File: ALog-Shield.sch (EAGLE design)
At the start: 28 parts, among them U1 DS3231MZ/V+T

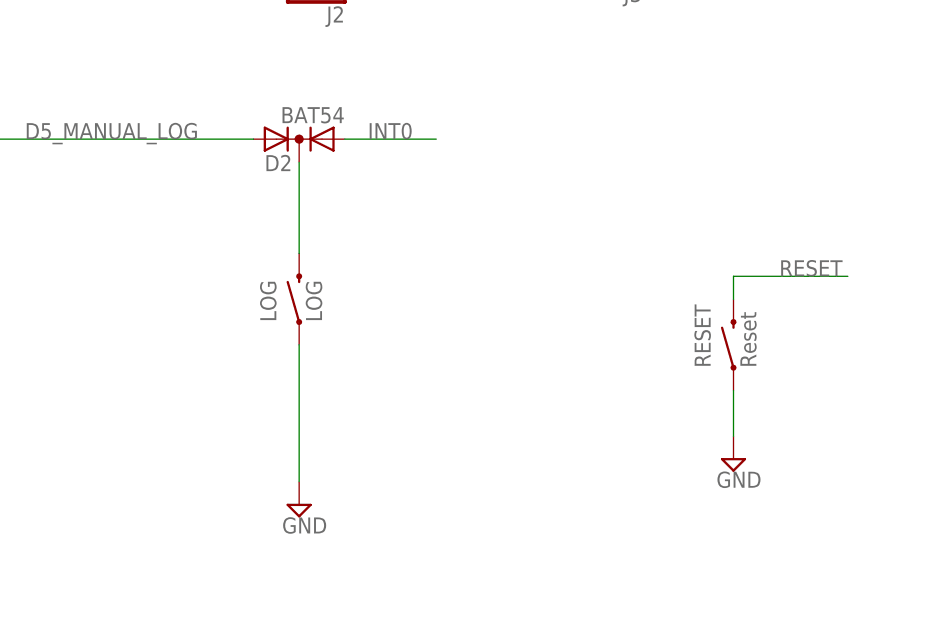
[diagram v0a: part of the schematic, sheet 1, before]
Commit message: New buttons: consistent with TLog
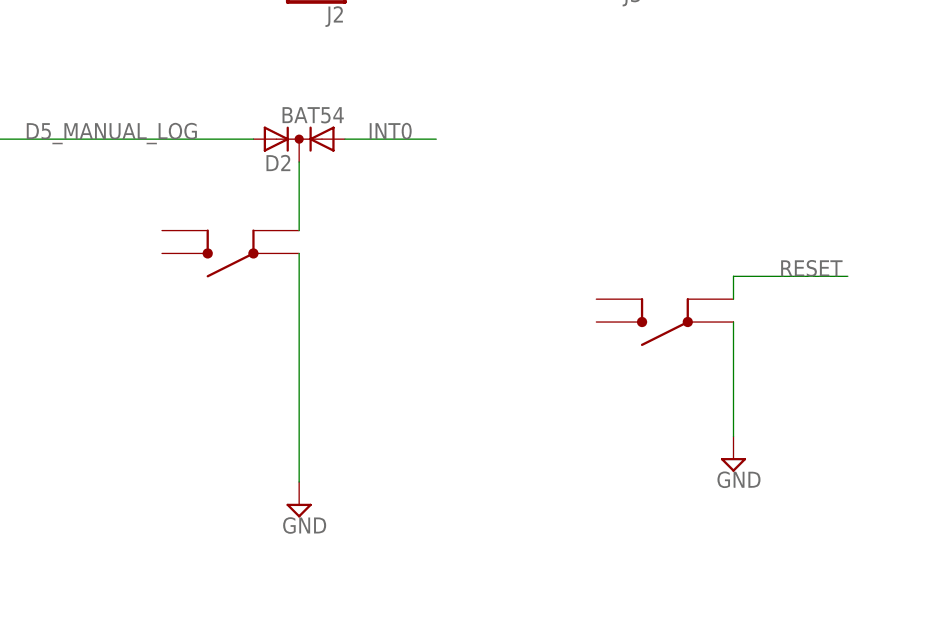
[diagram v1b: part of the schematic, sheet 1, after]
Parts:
- LOG, RESET: device SparkFun-Electromechanical:SWITCH-MOMENTARY-2PTH -> bschulz:BUTTON4.2X3.2
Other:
- note added: "JUMPER: REFERENCE ANALOG TO 3V3 INSTEAD OF VCC"
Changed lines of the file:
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@@
 <part name="SUPPLY47" library="supply2" deviceset="GND" device=""/>
 <part name="SUPPLY52" library="supply2" deviceset="GND" device=""/>
-<part name="RESET" library="SparkFun-Electromechanical" deviceset="SWITCH-MOMENTARY-2" device="PTH" value="Reset"/>
+<part name="RESET" library="bschulz" deviceset="BUTTON" device="4.2X3.2" value="Reset"/>
 <part name="SUPPLY53" library="supply2" deviceset="GND" device=""/>
 <part name="CLOCK_BATT_DECOUP" library="rcl" deviceset="C-EU" device="C0603" value="0.1uF"/>
 <part name="SUPPLY56" library="supply2" deviceset="GND" device=""/>
 <part name="D2" library="semicon-smd-ipc" deviceset="DIODE_AC-CA_" device="" value="BAT54"/>
-<part name="LOG" library="SparkFun-Electromechanical" deviceset="SWITCH-MOMENTARY-2" device="PTH" value="LOG"/>
+<part name="LOG" library="bschulz" deviceset="BUTTON" device="4.2X3.2" value="LOG"/>
 <part name="U1" library="Maxim-DS3231MZ_8-SOIC" deviceset="DS3231MZ/V+T" device=""/>
 <part name="FRAME1" library="frames" deviceset="LETTER_P" device=""/>
@@
 <instance part="SUPPLY47" gate="GND" x="20.32" y="-177.8"/>
 <instance part="SUPPLY52" gate="GND" x="109.22" y="-200.66"/>
-<instance part="RESET" gate="G$1" x="157.48" y="-182.88" rot="R90"/>
+<instance part="RESET" gate="G$1" x="157.48" y="-180.34" rot="R180"/>
 <instance part="SUPPLY53" gate="GND" x="63.5" y="-208.28"/>
 <instance part="D2" gate="G$1" x="109.22" y="-160.02" rot="R180"/>
-<instance part="LOG" gate="G$1" x="109.22" y="-177.8" rot="R90"/>
+<instance part="LOG" gate="G$1" x="109.22" y="-172.72" rot="R180"/>
 <instance part="FRAME1" gate="G$1" x="0" y="-248.92"/>
 <instance part="FRAME1" gate="G$2" x="83.82" y="-248.92" smashed="yes">
@@
 </segment>
 <segment>
-<wire x1="157.48" y1="-187.96" x2="157.48" y2="-193.04" width="0.1524" layer="91"/>
+<wire x1="157.48" y1="-180.34" x2="157.48" y2="-193.04" width="0.1524" layer="91"/>
 <pinref part="SUPPLY31" gate="GND" pin="GND"/>
 <pinref part="RESET" gate="G$1" pin="1"/>
@@
 <segment>
 <pinref part="SUPPLY52" gate="GND" pin="GND"/>
-<wire x1="109.22" y1="-182.88" x2="109.22" y2="-198.12" width="0.1524" layer="91"/>
+<wire x1="109.22" y1="-172.72" x2="109.22" y2="-198.12" width="0.1524" layer="91"/>
 <pinref part="LOG" gate="G$1" pin="1"/>
 </segment>
@@
 <pinref part="LOG" gate="G$1" pin="2"/>
 <pinref part="D2" gate="G$1" pin="K"/>
-<wire x1="109.22" y1="-172.72" x2="109.22" y2="-162.56" width="0.1524" layer="91"/>
+<wire x1="109.22" y1="-170.18" x2="109.22" y2="-162.56" width="0.1524" layer="91"/>
 </segment>
 </net>
@@
 <text x="90.17" y="26.416" size="5.08" layer="97">ALOG</text>
 <text x="170.942" y="1.016" size="2.54" layer="97">2/2</text>
-<wire x1="0" y1="81.28" x2="185.42" y2="81.28" width="0.1524" layer="97" style="dashdot"/>
+<wire x1="0" y1="81.28" x2="104.14" y2="81.28" width="0.1524" layer="97" style="dashdot"/>
 <text x="152.4" y="27.94" size="1.778" layer="97">Andrew Wickert
 Chad Sandell</text>
@@
 http://creativecommons.org/licenses/by-sa/3.0
 Design by: Andrew D. Wickert and Chad T. Sandell</text>
+<wire x1="104.14" y1="81.28" x2="185.42" y2="81.28" width="0.1524" layer="97" style="dashdot"/>
+<wire x1="104.14" y1="35.56" x2="104.14" y2="81.28" width="0.1524" layer="97" style="dashdot"/>
+<text x="114.3" y="76.2" size="1.778" layer="97">JUMPER: REFERENCE ANALOG TO 3V3 INSTEAD OF VCC</text>
 </plain>
 <instances>

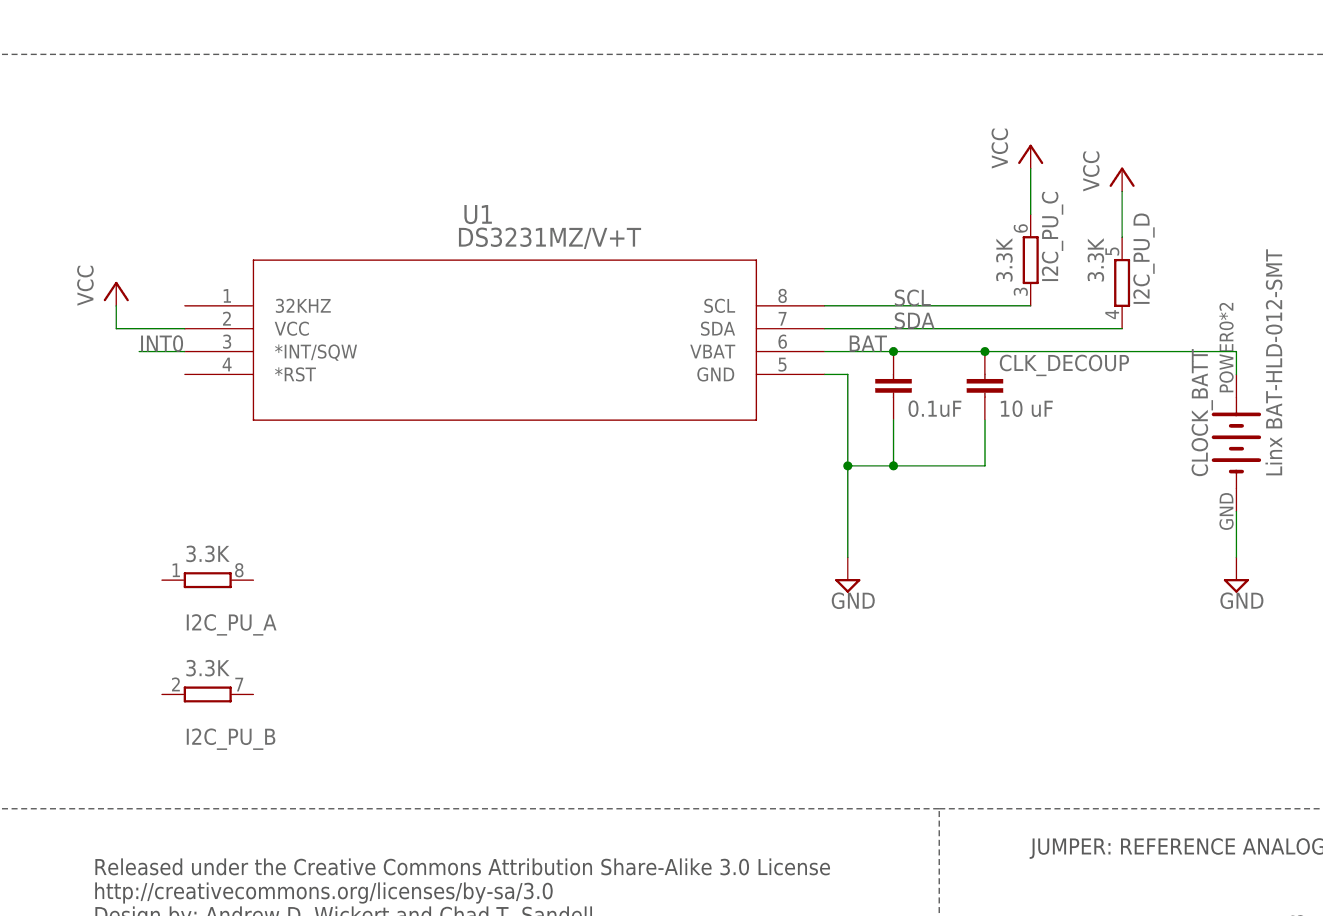
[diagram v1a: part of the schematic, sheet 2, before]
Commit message: 3.3K RTC PU array to discrete (10K?)
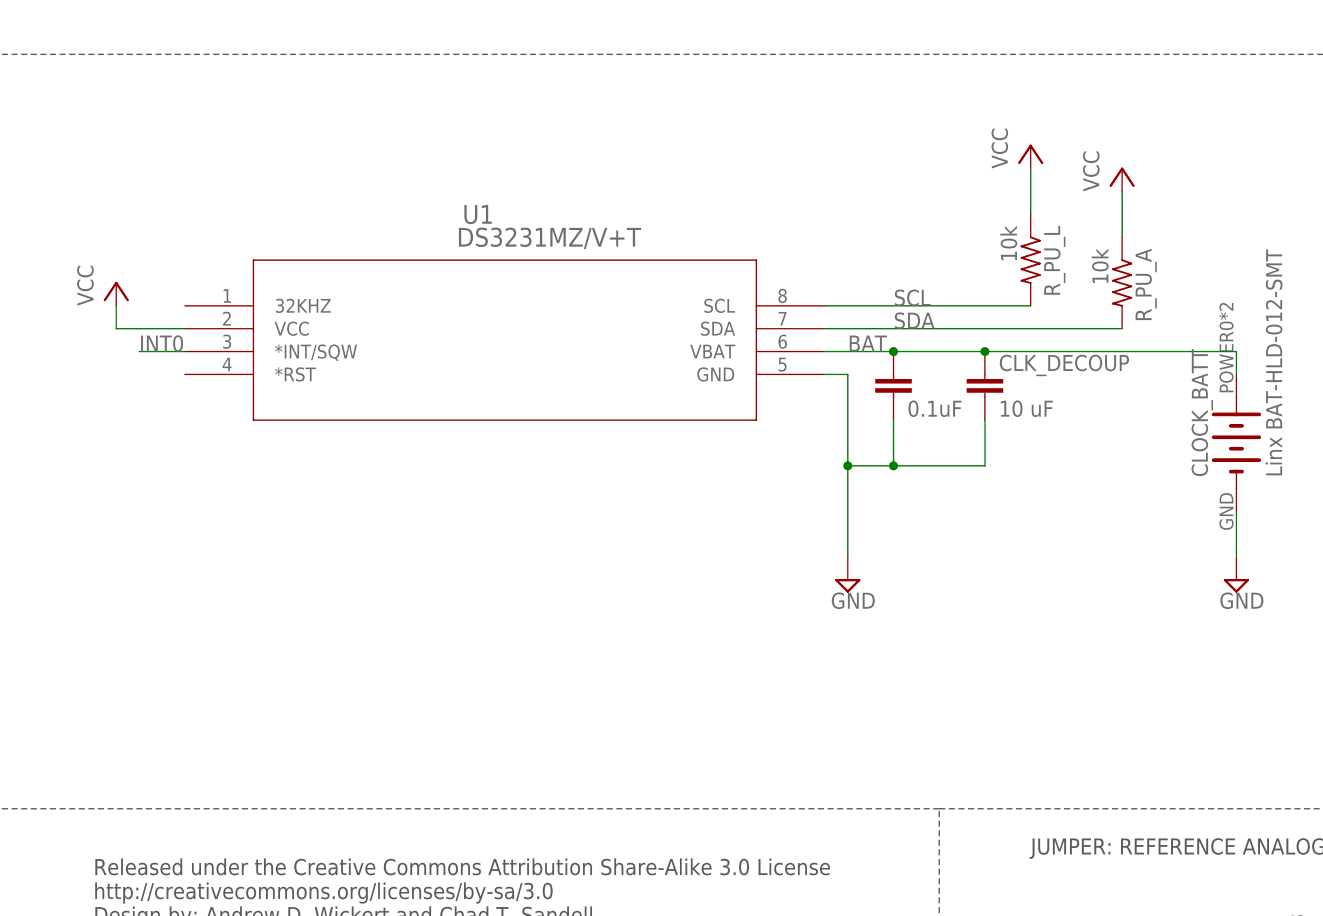
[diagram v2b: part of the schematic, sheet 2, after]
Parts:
- removed I2C_PU_: 3.3K, resistor-dil:4R-N0603-ARC
- added R_PU_A, R_PU_L: 10k, resistor:R-US_R0603
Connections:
- net SCL: now also R_PU_L.2; no longer I2C_PU_C.1
- net SDA: now also R_PU_A.2; no longer I2C_PU_D.1
- net VCC: now also R_PU_A.1, R_PU_L.1; no longer I2C_PU_C.2, I2C_PU_D.2
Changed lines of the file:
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@@
 <?xml version="1.0" encoding="utf-8"?>
 <!DOCTYPE eagle SYSTEM "eagle.dtd">
-<eagle version="8.3.1">
+<eagle version="8.5.0">
 <drawing>
 <settings>
@@
 <part name="SUPPLY3" library="supply2" deviceset="GND" device=""/>
 <part name="J2" library="SparkFun-Connectors" deviceset="CONN_04" device="SCREW"/>
-<part name="I2C_PU_" library="resistor-dil" deviceset="4R-N" device="0603-ARC" value="3.3K"/>
 <part name="C15" library="rc-master-smd" deviceset="CCA_" device="" value="10nF"/>
 <part name="CLOCK_BATT" library="awickert" deviceset="LINX-BAT-HLD-012-SMT-OTL" device="" value="Linx BAT-HLD-012-SMT"/>
@@
 <part name="JP1" library="SparkFun-Connectors" deviceset="M02" device="LOCK"/>
 <part name="+3V3" library="supply1" deviceset="+3V3" device=""/>
+<part name="R_PU_L" library="resistor" deviceset="R-US_" device="R0603" value="10k"/>
+<part name="R_PU_A" library="resistor" deviceset="R-US_" device="R0603" value="10k"/>
 </parts>
 <sheets>
@@
 <instance part="P+7" gate="VCC" x="114.3" y="154.94"/>
 <instance part="P+9" gate="VCC" x="12.7" y="139.7"/>
-<instance part="I2C_PU_" gate="A" x="22.86" y="106.68" smashed="yes">
-<attribute name="VALUE" x="20.32" y="108.712" size="1.778" layer="96"/>
-<attribute name="NAME" x="20.32" y="101.092" size="1.778" layer="95"/>
-</instance>
-<instance part="I2C_PU_" gate="B" x="22.86" y="93.98" smashed="yes">
-<attribute name="VALUE" x="20.32" y="96.012" size="1.778" layer="96"/>
-<attribute name="NAME" x="20.32" y="88.392" size="1.778" layer="95"/>
-</instance>
-<instance part="I2C_PU_" gate="C" x="114.3" y="142.24" smashed="yes" rot="R90">
-<attribute name="VALUE" x="112.268" y="139.7" size="1.778" layer="96" rot="R90"/>
-<attribute name="NAME" x="117.348" y="139.7" size="1.778" layer="95" rot="R90"/>
-</instance>
-<instance part="I2C_PU_" gate="D" x="124.46" y="139.7" smashed="yes" rot="R90">
-<attribute name="VALUE" x="122.428" y="139.7" size="1.778" layer="96" rot="R90"/>
-<attribute name="NAME" x="127.508" y="137.16" size="1.778" layer="95" rot="R90"/>
-</instance>
 <instance part="CLOCK_BATT" gate="G$1" x="137.16" y="121.92" rot="R90"/>
 <instance part="+3V2" gate="G$1" x="60.96" y="215.9"/>
@@
 <instance part="JP1" gate="G$1" x="129.54" y="58.42"/>
 <instance part="+3V3" gate="G$1" x="147.32" y="68.58"/>
+<instance part="R_PU_L" gate="G$1" x="114.3" y="142.24" rot="R270"/>
+<instance part="R_PU_A" gate="G$1" x="124.46" y="139.7" rot="R270"/>
 </instances>
 <busses>
@@
 <wire x1="124.46" y1="149.86" x2="124.46" y2="144.78" width="0.1524" layer="91"/>
 <pinref part="P+5" gate="VCC" pin="VCC"/>
-<pinref part="I2C_PU_" gate="D" pin="2"/>
+<pinref part="R_PU_A" gate="G$1" pin="1"/>
 </segment>
 <segment>
 <wire x1="114.3" y1="152.4" x2="114.3" y2="147.32" width="0.1524" layer="91"/>
 <pinref part="P+7" gate="VCC" pin="VCC"/>
-<pinref part="I2C_PU_" gate="C" pin="2"/>
+<pinref part="R_PU_L" gate="G$1" pin="1"/>
 </segment>
 <segment>
@@
 <label x="99.06" y="137.16" size="1.778" layer="95"/>
 <pinref part="U1" gate="A" pin="SCL"/>
-<pinref part="I2C_PU_" gate="C" pin="1"/>
+<pinref part="R_PU_L" gate="G$1" pin="2"/>
 </segment>
 </net>
@@
 <label x="99.06" y="134.62" size="1.778" layer="95"/>
 <pinref part="U1" gate="A" pin="SDA"/>
-<pinref part="I2C_PU_" gate="D" pin="1"/>
-</segment>
-</net>
+<pinref part="R_PU_A" gate="G$1" pin="2"/>
+</segment>
+</net>

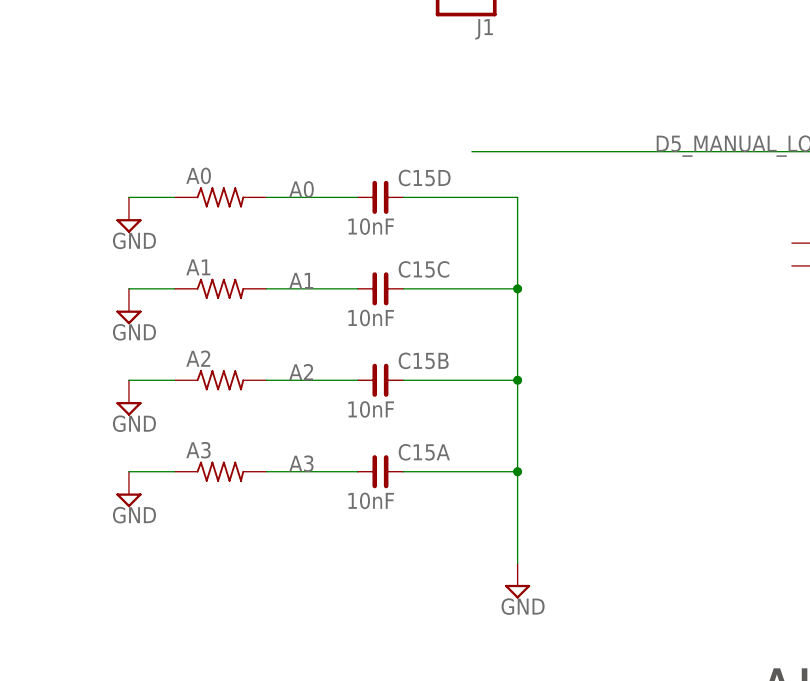
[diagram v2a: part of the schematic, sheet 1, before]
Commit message: rm cap array
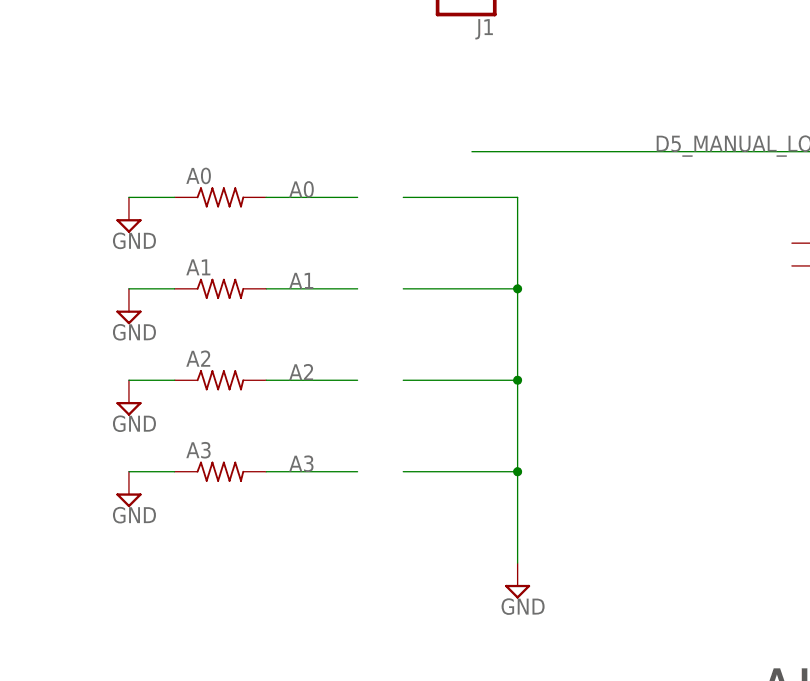
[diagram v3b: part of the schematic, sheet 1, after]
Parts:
- removed C15: 10nF, rc-master-smd:CCA_
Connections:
- net A0: no longer C15D.1
- net A1: no longer C15C.1
- net A2: no longer C15B.1
- net A3: no longer C15A.1
- net GND: no longer C15A.2, C15B.2, C15C.2, C15D.2
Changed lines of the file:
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@@
 <part name="SUPPLY3" library="supply2" deviceset="GND" device=""/>
 <part name="J2" library="SparkFun-Connectors" deviceset="CONN_04" device="SCREW"/>
-<part name="C15" library="rc-master-smd" deviceset="CCA_" device="" value="10nF"/>
 <part name="CLOCK_BATT" library="awickert" deviceset="LINX-BAT-HLD-012-SMT-OTL" device="" value="Linx BAT-HLD-012-SMT"/>
 <part name="U$2" library="awickert" deviceset="MADE_IN_MN_220_SHIELD" device=""/>
@@
 <instance part="SUPPLY3" gate="GND" x="73.66" y="-137.16"/>
 <instance part="J2" gate="G$1" x="109.22" y="-137.16" rot="R180"/>
-<instance part="C15" gate="A" x="48.26" y="-195.58"/>
-<instance part="C15" gate="B" x="48.26" y="-185.42"/>
-<instance part="C15" gate="C" x="48.26" y="-175.26"/>
-<instance part="C15" gate="D" x="48.26" y="-165.1"/>
 <instance part="U$2" gate="G$1" x="17.78" y="-233.68"/>
 <instance part="U$3" gate="G$1" x="25.4" y="-236.22"/>
@@
 <pinref part="SUPPLY53" gate="GND" pin="GND"/>
 <wire x1="63.5" y1="-165.1" x2="63.5" y2="-175.26" width="0.1524" layer="91"/>
-<pinref part="C15" gate="D" pin="2"/>
 <wire x1="63.5" y1="-175.26" x2="63.5" y2="-185.42" width="0.1524" layer="91"/>
 <wire x1="63.5" y1="-185.42" x2="63.5" y2="-195.58" width="0.1524" layer="91"/>
 <wire x1="63.5" y1="-195.58" x2="63.5" y2="-205.74" width="0.1524" layer="91"/>
 <wire x1="63.5" y1="-165.1" x2="50.8" y2="-165.1" width="0.1524" layer="91"/>
-<pinref part="C15" gate="C" pin="2"/>
 <wire x1="50.8" y1="-175.26" x2="63.5" y2="-175.26" width="0.1524" layer="91"/>
 <junction x="63.5" y="-175.26"/>
-<pinref part="C15" gate="B" pin="2"/>
 <wire x1="50.8" y1="-185.42" x2="63.5" y2="-185.42" width="0.1524" layer="91"/>
 <junction x="63.5" y="-185.42"/>
-<pinref part="C15" gate="A" pin="2"/>
 <wire x1="50.8" y1="-195.58" x2="63.5" y2="-195.58" width="0.1524" layer="91"/>
 <junction x="63.5" y="-195.58"/>
@@
 <segment>
 <pinref part="A2" gate="G$1" pin="2"/>
-<pinref part="C15" gate="B" pin="1"/>
 <wire x1="35.56" y1="-185.42" x2="45.72" y2="-185.42" width="0.1524" layer="91"/>
 <label x="38.1" y="-185.42" size="1.778" layer="95"/>
@@
 <segment>
 <pinref part="A0" gate="G$1" pin="2"/>
-<pinref part="C15" gate="D" pin="1"/>
 <wire x1="35.56" y1="-165.1" x2="45.72" y2="-165.1" width="0.1524" layer="91"/>
 <label x="38.1" y="-165.1" size="1.778" layer="95"/>
@@
 </segment>
 <segment>
-<pinref part="C15" gate="A" pin="1"/>
 <pinref part="A3" gate="G$1" pin="2"/>
 <wire x1="45.72" y1="-195.58" x2="35.56" y2="-195.58" width="0.1524" layer="91"/>
@@
 <segment>
 <pinref part="A1" gate="G$1" pin="2"/>
-<pinref part="C15" gate="C" pin="1"/>
 <wire x1="35.56" y1="-175.26" x2="45.72" y2="-175.26" width="0.1524" layer="91"/>
 <label x="38.1" y="-175.26" size="1.778" layer="95"/>
